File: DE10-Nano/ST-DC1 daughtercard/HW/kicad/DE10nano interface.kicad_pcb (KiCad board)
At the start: 2 copper layers, 200 x 155 mm, 122 parts, among them J1 DE0_ADC, J10 ENC1_IN, J11 Conn_In_13, J12 Conn_Out_1, J13 Conn_Out_0, J14 Conn_In_0, J15 Conn_In_1, J16 StepGen4, J17 StepGen0, J18 StepGen2, J19 StepGen1, J2 DE0_GPIO_0, J20 StepGen3, J21 StepGen5, J22 Conn_Field+, J23 Conn_In_14, J24 Conn_In_15, J25 Conn_01x08-Connector_Generic, J27 ENC2_IN, J3 ENC0_IN, J30 ENC3_IN, J33 ENC4_IN, J36 ENC5_IN, J39 Conn_ADC_1_10V, J4 Conn_In_8, J41 Conn_Opto_out, J42 Conn_ADC_0_5V, J43 Conn_Fan, J45 Conn_In_2, J46 Conn_RS422, J47 Conn_VIN, J48 Conn_5v, J49 Conn_In_3, J5 Conn_In_9, J50 Conn_In_4, J51 Conn_In_5, J52 Conn_In_6, J53 Conn_In_7, J6 DE0_GPIO_1, J7 Conn_In_10, J8 Conn_In_11, J9 Conn_In_12, U1 AM26LS32, U10 AM26LS32, U11 AM26LS32, U12 AM26LS32, U13 AM26LS32, U14 MIC2981, U15 LM22679, U16 SMP-1A36-6S, U17 SMP-1A36-6S, U18 MIC2981, U19 74LVC2G04, U2 AM26LS32, U3 DS89C21, U4 MIC2981, U5 ULN2803A, U6 ULN2803A, U7 SN75174DWR, U8 SN75174DWR, U9 SN75174DWR

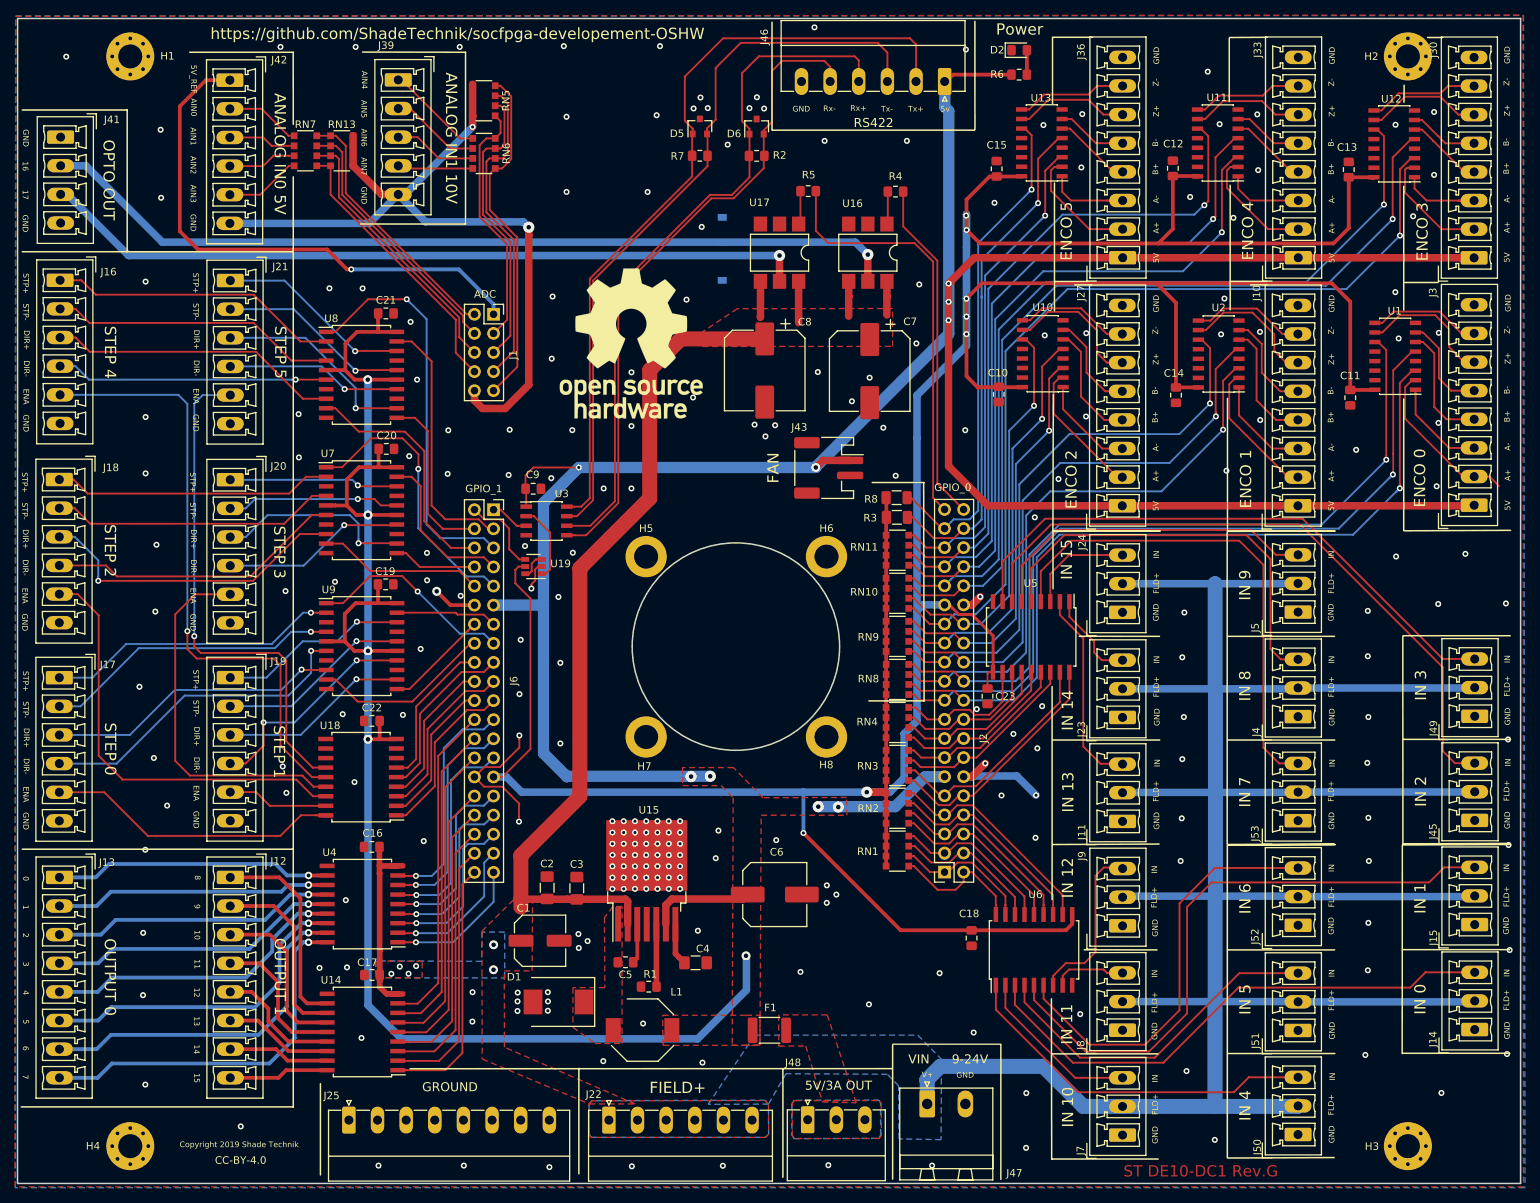
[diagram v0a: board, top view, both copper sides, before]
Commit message: Add Artwork to PCB:   DE10-Nano/ST-DC1 daughtercard/HW/kicad/DE10nano interface-cache.lib 	Add Artwork to PCB:    DE10-Nano/ST-DC1 daughtercard/HW/kicad/DE10nano interface.jpg 	Add termination Resistors to diff inputs:   DE10-Nano/ST-DC1 daughtercard/HW/kicad/DE10nano interface.kicad_pcb 	Add termination Resistors to diff inputs:   DE10-Nano/ST-DC1 daughtercard/HW/kicad/DE10nano interface.kicad_pcb-bak 	Add termination Resistors to diff inputs:   DE10-Nano/ST-DC1 daughtercard/HW/kicad/DE10nano interface.net 	Add termination Resistors to diff inputs:   DE10-Nano/ST-DC1 daughtercard/HW/kicad/DE10nano interface.pro 	Add termination Resistors to diff inputs:   DE10-Nano/ST-DC1 daughtercard/HW/kicad/Images/DE10nano interface back.jpg 	Add Artwork to PCB:   DE10-Nano/ST-DC1 daughtercard/HW/kicad/Images/DE10nano interface.jpg 	Reflect incomplete BOM:    DE10-Nano/ST-DC1 daughtercard/HW/kicad/bom/BOM.ods -> DE10-Nano/ST-DC1 daughtercard/HW/kicad/bom/BOM-incomplete-use-ibom.ods 	Add termination Resistors to diff inputs:   DE10-Nano/ST-DC1 daughtercard/HW/kicad/bom/ibom.html 	Add termination Resistors to diff inputs:   DE10-Nano/ST-DC1 daughtercard/HW/kicad/file5CE4621E.sch 	Add termination Resistors to diff inputs:   DE10-Nano/ST-DC1 daughtercard/HW/kicad/file5CE4621E.sch-bak 	Add termination Resistors to diff inputs:   DE10-Nano/ST-DC1 daughtercard/HW/kicad/file5D10B445.sch-bak 	Add termination Resistors to diff inputs:   DE10-Nano/ST-DC1 daughtercard/HW/kicad/file5D22A4F0.sch 	modified:   DE10-Nano/ST-DC1 daughtercard/HW/kicad/file5D22A4F0.sch-bak 	modified:   DE10-Nano/ST-DC1 daughtercard/HW/kicad/gerbers rev_G.zip 	modified:   DE10-Nano/ST-DC1 daughtercard/HW/kicad/gerbers rev_G/DE10nano interface-B_Cu.gbr 	modified:   DE10-Nano/ST-DC1 daughtercard/HW/kicad/gerbers rev_G/DE10nano interface-B_Mask.gbr 	modified:   DE10-Nano/ST-DC1 daughtercard/HW/kicad/gerbers rev_G/DE10nano interface-B_Paste.gbr 	modified:   DE10-Nano/ST-DC1 daughtercard/HW/kicad/gerbers rev_G/DE10nano i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
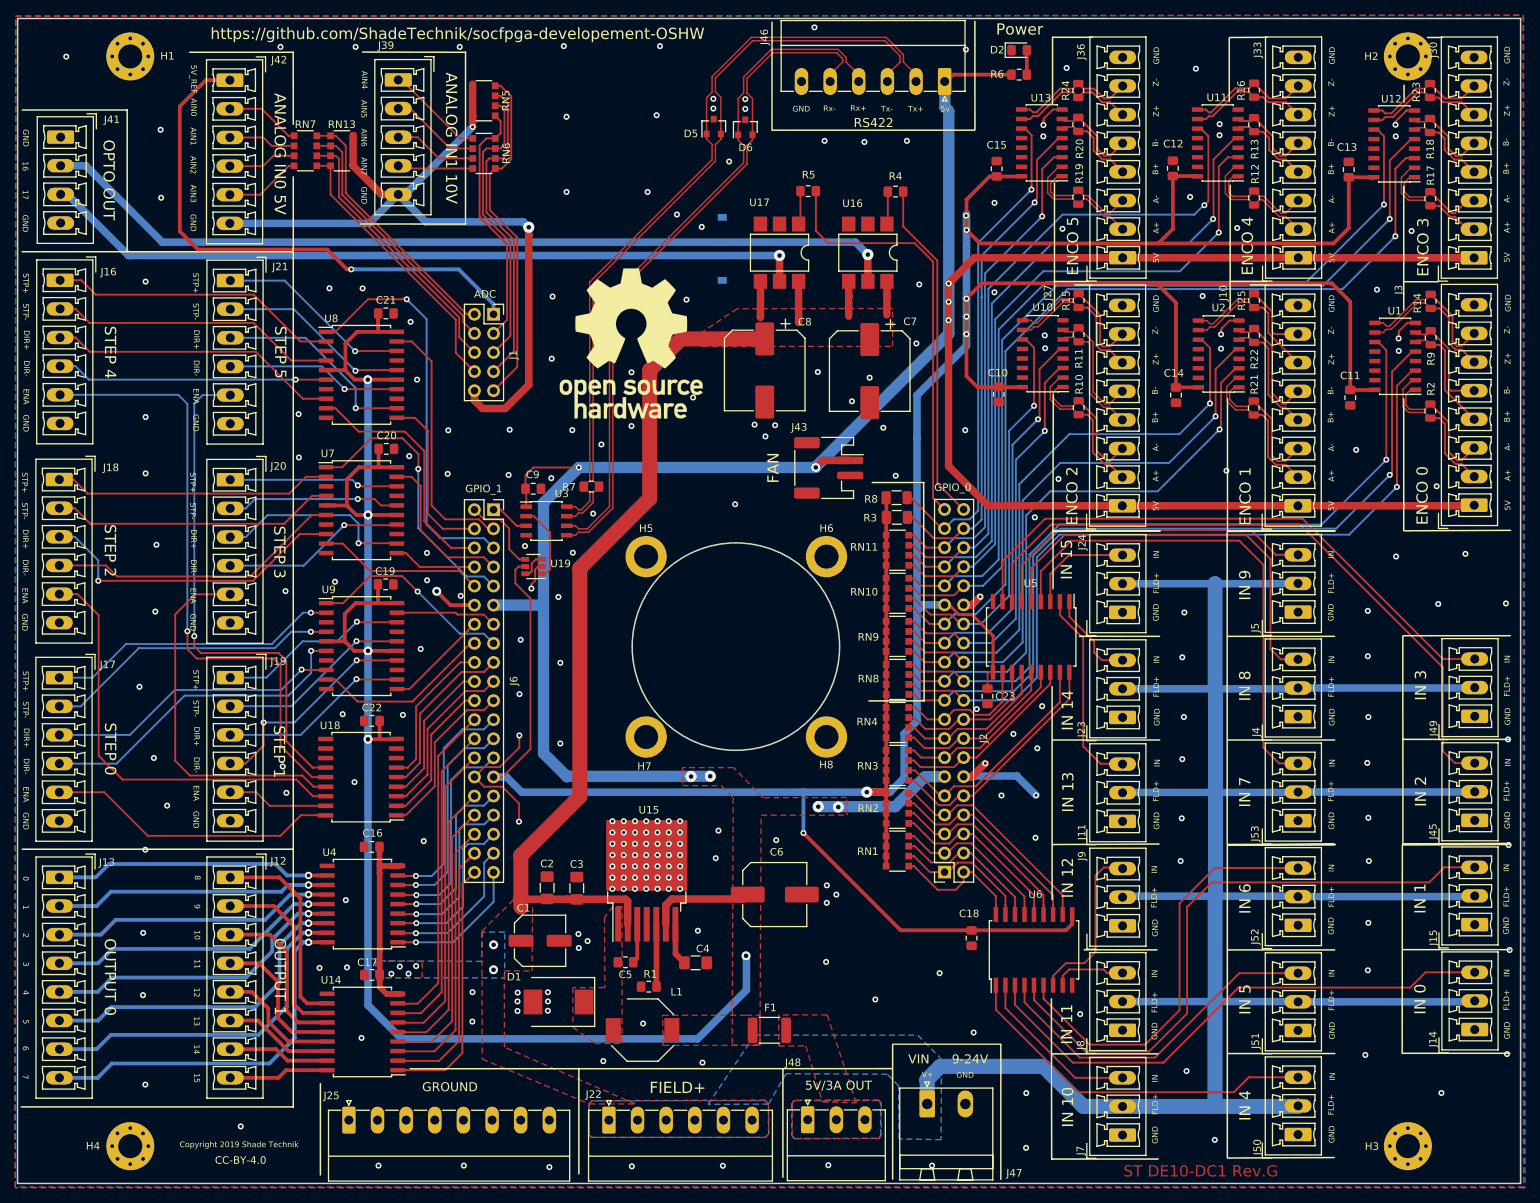
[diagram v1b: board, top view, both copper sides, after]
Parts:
- removed the REF** at (141.3, 153.5)
- added R10: 120R, Resistor_SMD:R_0805_2012Metric, F.Cu at (168.3, 68.5)
- added R11: 120R, Resistor_SMD:R_0805_2012Metric, F.Cu at (168.3, 58.9)
- added R12: 120R, Resistor_SMD:R_0805_2012Metric, F.Cu at (191.7, 40.6)
- added R13: 120R, Resistor_SMD:R_0805_2012Metric, F.Cu at (191.7, 30.9)
- added R14: 120R, Resistor_SMD:R_0805_2012Metric, F.Cu at (215.2, 54.4)
- added R15: 120R, Resistor_SMD:R_0805_2012Metric, F.Cu at (168.3, 54.3)
- added R16: 120R, Resistor_SMD:R_0805_2012Metric, F.Cu at (191.7, 26.3)
- added R17: 120R, Resistor_SMD:R_0805_2012Metric, F.Cu at (215.2, 40.8)
- added R18: 120R, Resistor_SMD:R_0805_2012Metric, F.Cu at (215.1, 31.0)
- added R19: 120R, Resistor_SMD:R_0805_2012Metric, F.Cu at (168.3, 40.5)
- added R20: 120R, Resistor_SMD:R_0805_2012Metric, F.Cu at (168.3, 30.9)
- added R21: 120R, Resistor_SMD:R_0805_2012Metric, F.Cu at (191.7, 68.6)
- added R22: 120R, Resistor_SMD:R_0805_2012Metric, F.Cu at (191.7, 58.9)
- added R23: 120R, Resistor_SMD:R_0805_2012Metric, F.Cu at (215.1, 26.4)
- added R24: 120R, Resistor_SMD:R_0805_2012Metric, F.Cu at (168.3, 26.4)
- added R25: 120R, Resistor_SMD:R_0805_2012Metric, F.Cu at (191.7, 54.3)
- added R9: 120R, Resistor_SMD:R_0805_2012Metric, F.Cu at (215.2, 59.2)
- added REF**: Symbol_CreativeCommons_SilkScreenTop_Type2_Big, Symbol:Symbol_CreativeCommons_SilkScreenTop_Type2_Big, B.Cu at (151.8, 142.2)
- R2: footprint Resistor_SMD:R_0805_2012Metric_Pad1.15x1.40mm_HandSolder -> Resistor_SMD:R_0805_2012Metric
- moved R2 95.9 mm to (215.2, 69.0), turned to 270 degrees
- moved R7 46.3 mm to (103.5, 79.0)
- moved D5 1.85 mm to (119.8, 31.1)
- moved D6 1.51 mm to (124.0, 31.2)
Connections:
- R2 pad 1: /RS422 Interface/Tx+ -> ENC0_CHAN_A-
- R2 pad 2: /RS422 Interface/Tx- -> ENC0_CHAN_A+
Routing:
- net DGND: track 45.7 -> 60.2 mm, vias 246 -> 245
- net ENC2_CHAN_A-: track 13.0 -> 18.8 mm
- net ENC1_CHAN_A-: track 13.4 -> 19.1 mm
- net ENC2_CHAN_Z-: track 15.4 -> 21.0 mm
- net ENC0_CHAN_Z-: track 15.0 -> 20.6 mm
- net ENC0_CHAN_A-: track 13.2 -> 18.7 mm
- net ENC5_CHAN_A-: track 10.6 -> 15.1 mm
- net ENC4_CHAN_A-: track 10.3 -> 14.7 mm
- net /RS422 Interface/Tx+: track 87.1 -> 91.0 mm
- net ENC2_CHAN_B-: track 13.3 -> 17.0 mm
- net ENC1_CHAN_Z-: track 15.3 -> 18.9 mm
- net ENC1_CHAN_B-: track 13.5 -> 16.7 mm
- net /RS422 Interface/Rx-: track 104.1 -> 101.0 mm
- net ENC5_CHAN_B-: track 9.38 -> 12.1 mm
- net /RS422 Interface/Rx+: track 97.5 -> 100.3 mm
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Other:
- net class 0.5mm added: clearance 0.3, trace_width 0.5, via_dia 0.8, via_drill 0.4
